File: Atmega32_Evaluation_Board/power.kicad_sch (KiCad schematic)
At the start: 19 parts, among them J1 Barrel_Jack_Switch, U1 LM1117MP-5.0, U2 LM1117MP-3.3

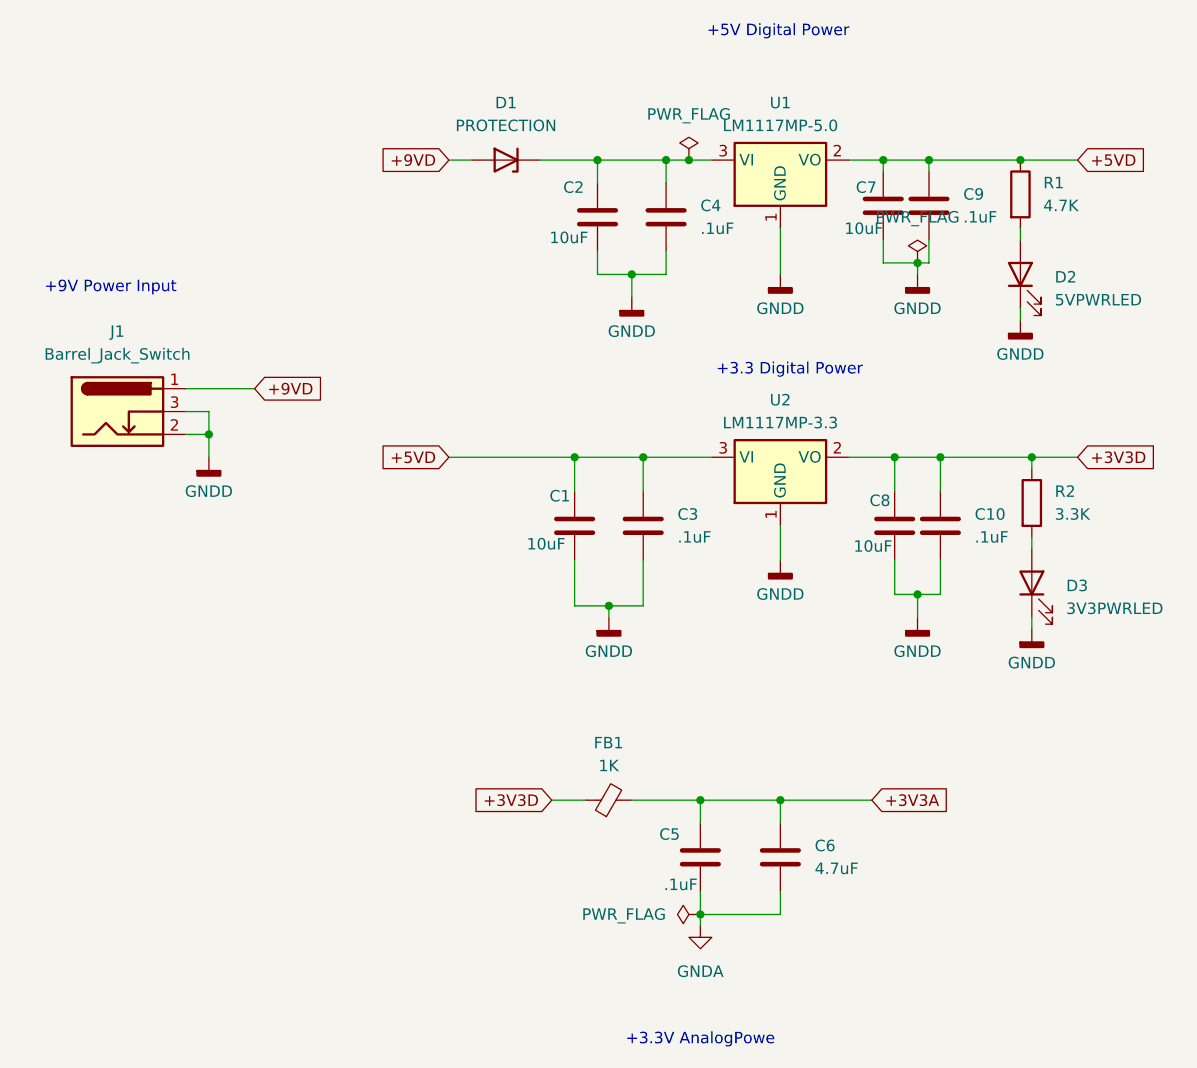
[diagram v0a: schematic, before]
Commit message: added Atmega project
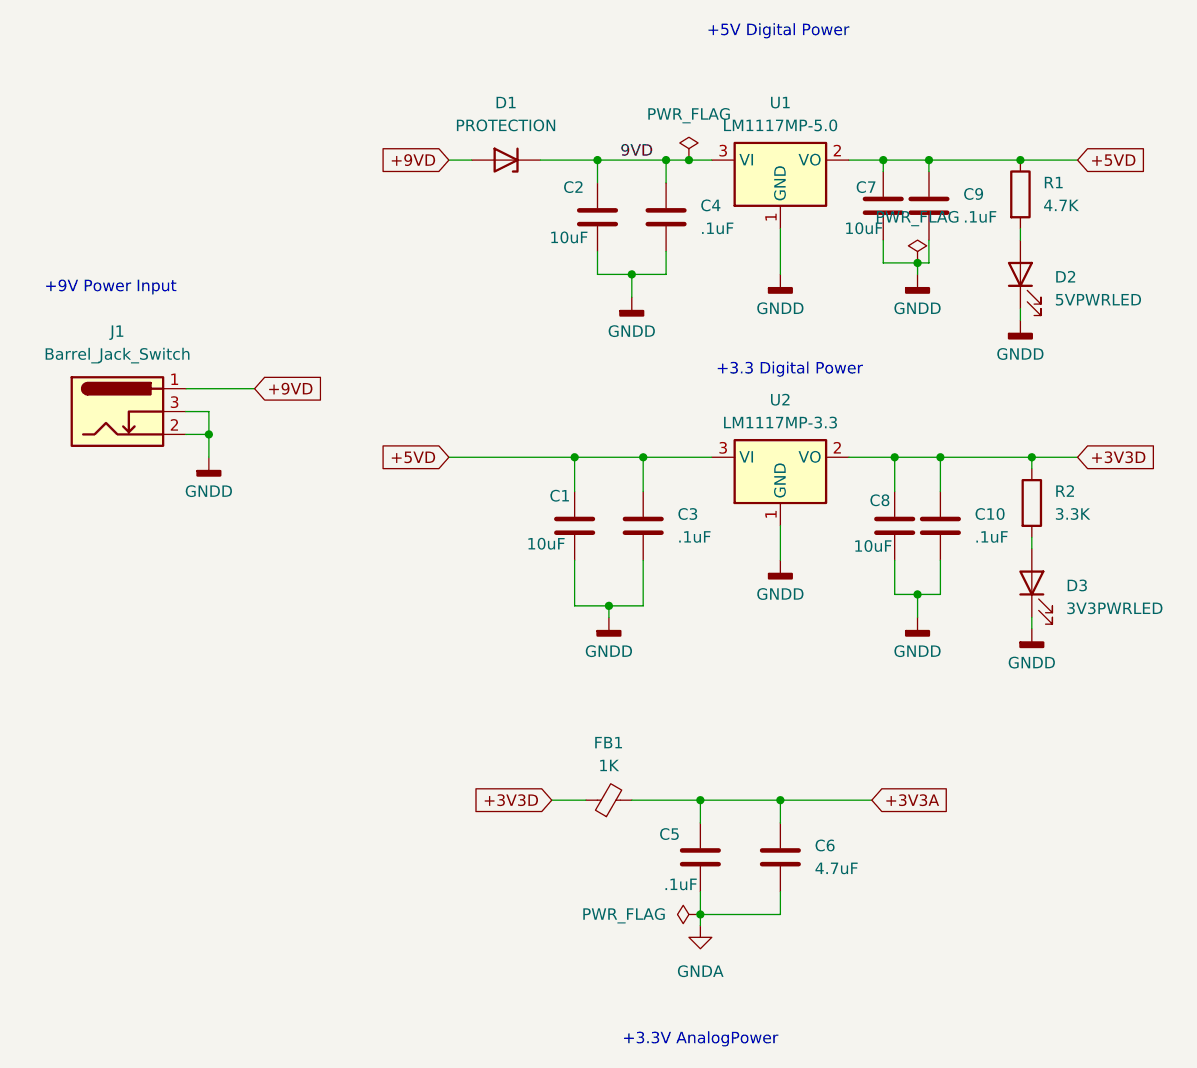
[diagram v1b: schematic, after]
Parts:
- J1: footprint Connector_BarrelJack:BarrelJack_CUI_PJ-079BH_Horizontal -> Connector_BarrelJack:BarrelJack_Horizontal
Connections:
- net 9VD: now reaches C2.1, C4.1, D1.1 (K), U1.3 (VI)
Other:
- note added: "+3.3V AnalogPower"
- note removed: "+3.3V AnalogPowe"
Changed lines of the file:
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@@
 		)
 	)
-	(text "+3.3V AnalogPowe"
+	(text "+3.3V AnalogPower\n"
 		(exclude_from_sim no)
 		(at 137.16 154.94 0)
@@
 			(width 0)
 			(type default)
+		)
+	)
+	(label "9VD"
+		(at 128.27 57.15 0)
+		(effects
+			(font
+				(size 1.27 1.27)
+			)
+			(justify left bottom)
 		)
 	)
@@
 			)
 		)
-		(property "Footprint" "Connector_BarrelJack:BarrelJack_CUI_PJ-079BH_Horizontal"
+		(property "Footprint" "Connector_BarrelJack:BarrelJack_Horizontal"
 			(at 73.66 86.106 0)
 			(effects
